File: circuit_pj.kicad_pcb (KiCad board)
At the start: 2 copper layers, 94.5 x 45.2 mm, 42 parts, among them J1 PWR, J2 Comm, J3 Drive_pin, J4 9V, Q1 2N3904, Q2 2N3904, Q3 2N3906, Q4 2N3904, Q5 2N3906, SW1 PWR_S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

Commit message: changed reset pin from a switch to a jumper, also reorganized the schematic
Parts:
- removed G*** (x2): LOGO, Pinger:test2
- removed REF** (x2): Pin_D1.0mm_L10.0mm, Connector_Pin:Pin_D1.0mm_L10.0mm
- removed SW2: RST_S, Button_Switch_THT:SW_DIP_SPSTx01_Slide_6.7x4.1mm_W7.62mm_P2.54mm_LowProfile
- added J5: Conn_01x02, Connector_PinHeader_2.54mm:PinHeader_1x02_P2.54mm_Vertical, F.Cu at (124.2, 83.8)
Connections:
- net /OSC1 renamed Net-(C5-Pad1)
- net /OSC2 renamed Net-(C6-Pad2)
- net /Reset renamed Reset
- net /Switch renamed Switch
- C1 pad 2: +9V -> Net-(C1-Pad2)
- SW1 pad 2: +9V -> Net-(C1-Pad2)
- U1 pad 1: +9V -> Net-(C1-Pad2)
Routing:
- net Net-(C1-Pad2): track 0.00 -> 29.5 mm, vias 0 -> 1
- net +9V: track 16.5 -> 0.00 mm, vias 1 -> 0
- net Net-(J5-Pad2): track 12.6 -> 7.03 mm
- net Reset: track 23.0 -> 24.4 mm

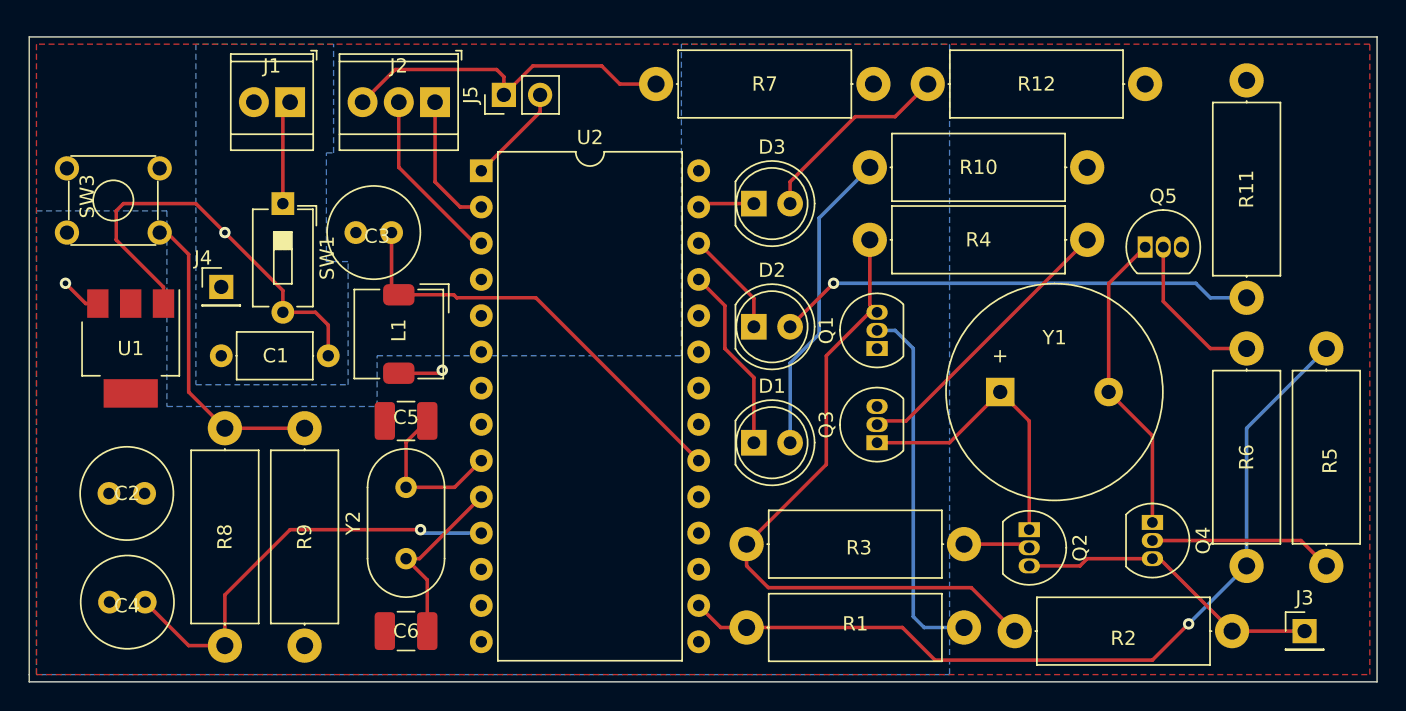
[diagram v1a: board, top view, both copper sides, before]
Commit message: adjusted sch and pcb after ltspice simulation, switched PNP and NPN positions and also connected the piezo to the collector pins instead of the emitters.
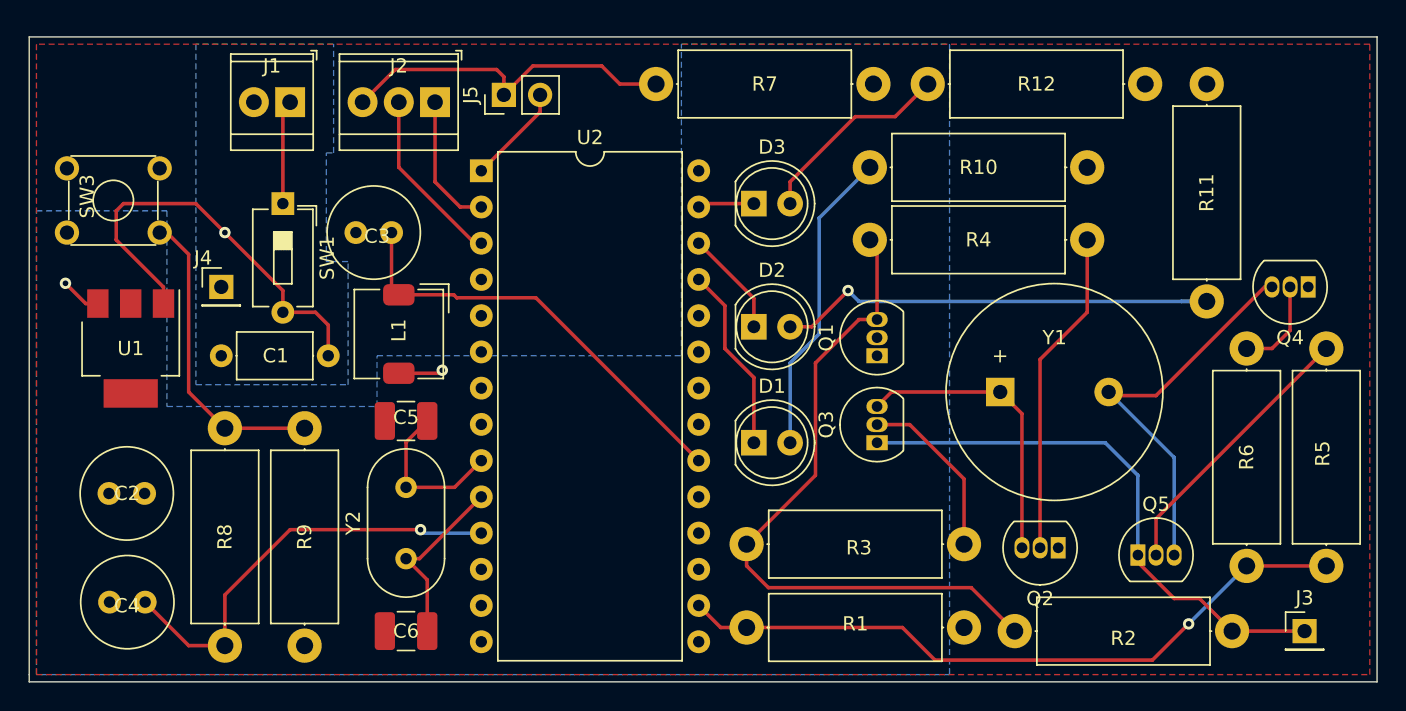
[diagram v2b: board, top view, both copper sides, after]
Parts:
- moved Q5 21.6 mm to (168.7, 116.1)
- moved Q4 19.8 mm to (180.6, 97.3), turned to 180 degrees
- moved R5 15.2 mm to (181.9, 101.6), turned to 270 degrees
- moved R11 2.81 mm to (173.5, 98.3)
- moved Q2 2.40 mm to (163.1, 115.6), turned to 180 degrees
- moved Q1 0.51 mm to (150.4, 102.1)
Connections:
- Q2 pad 1: Net-(Q2-Pad1) -> GND
- Q2 pad 3: Net-(J3-Pad1) -> Net-(Q2-Pad3)
- Q3 pad 1: Net-(Q2-Pad1) -> Net-(J3-Pad1)
- Q3 pad 3: GND -> Net-(Q2-Pad3)
- Q4 pad 1: Net-(Q4-Pad1) -> GND
- Q4 pad 3: Net-(J3-Pad1) -> Net-(Q4-Pad3)
- Q5 pad 1: Net-(Q4-Pad1) -> Net-(J3-Pad1)
- Q5 pad 3: GND -> Net-(Q4-Pad3)
- R3 pad 1: Net-(Q2-Pad2) -> Net-(Q3-Pad2)
- R4 pad 2: Net-(Q3-Pad2) -> Net-(Q2-Pad2)
- R5 pad 1: Net-(Q4-Pad2) -> Net-(Q5-Pad2)
- R6 pad 2: Net-(Q5-Pad2) -> Net-(Q4-Pad2)
- Y1 pad 1: Net-(Q2-Pad1) -> Net-(Q2-Pad3)
- Y1 pad 2: Net-(Q4-Pad1) -> Net-(Q4-Pad3)
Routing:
- net Net-(Q4-Pad3): track 0.00 -> 28.0 mm
- net Net-(Q1-Pad2): track 25.7 -> 0.00 mm
- net Net-(Q4-Pad1): track 21.6 -> 0.00 mm
- net Net-(Q2-Pad3): track 0.00 -> 20.6 mm
- net Net-(Q2-Pad1): track 20.6 -> 0.00 mm
- net Net-(Q2-Pad2): track 4.68 -> 23.0 mm
- net Net-(J3-Pad1): track 21.6 -> 39.0 mm
- net /Transmitter: track 60.3 -> 48.3 mm
- net Net-(Q5-Pad2): track 11.0 -> 19.4 mm
- net Net-(Q3-Pad2): track 20.1 -> 12.2 mm
- net Net-(Q4-Pad2): track 12.9 -> 6.62 mm
- net Net-(D2-Pad2): track 33.7 -> 31.6 mm
